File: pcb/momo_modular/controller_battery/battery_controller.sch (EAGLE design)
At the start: 33 parts, among them U1 XRP7659, U2 MAX1555, U3 MCP1702, U4 PIC24F16KA101-X_PSSOP, U5 FLASH8MSOP8

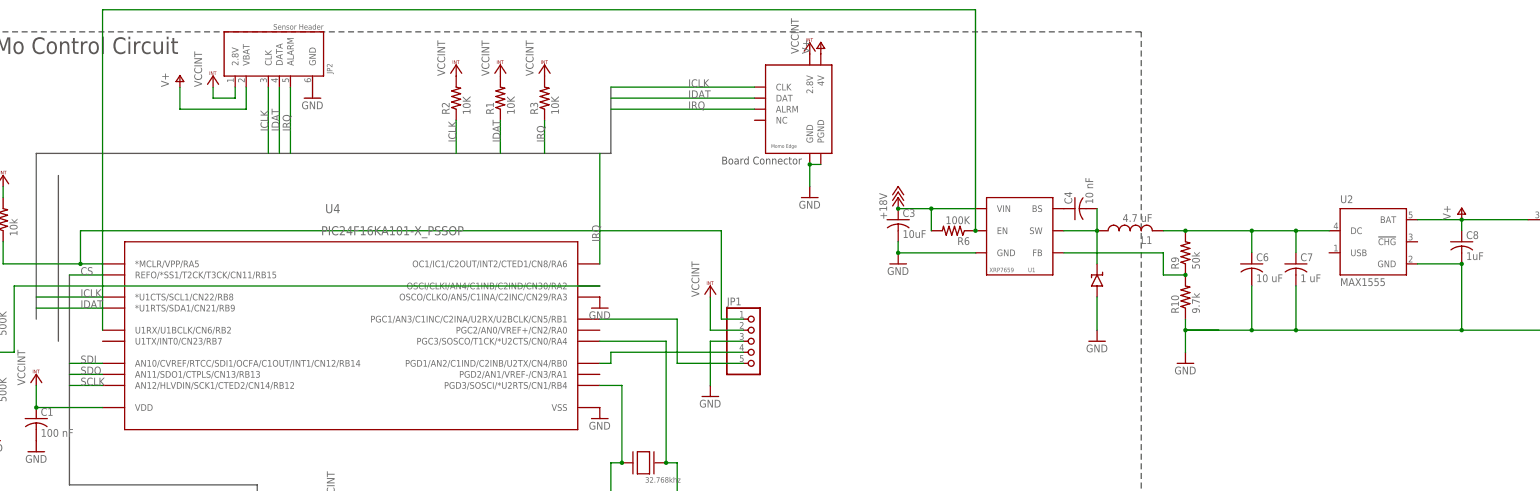
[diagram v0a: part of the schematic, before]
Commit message: Begin work on resource manager and revised task manager on pic24.  Started relaying out controller board and combining functionality.
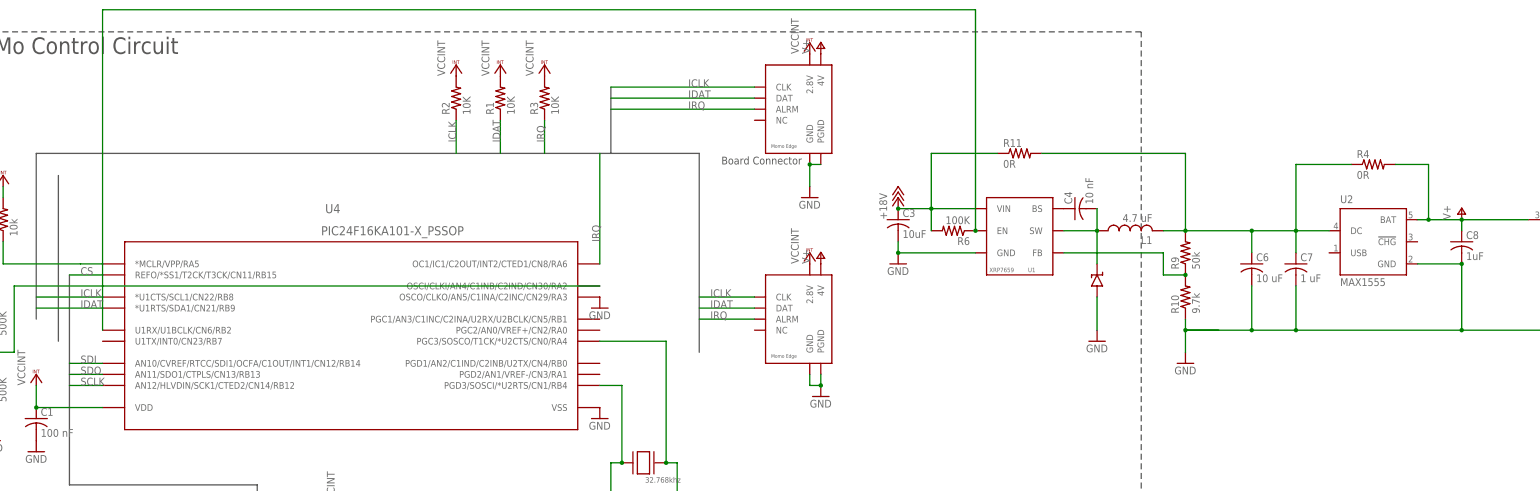
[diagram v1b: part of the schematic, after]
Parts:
- removed JP2: MOMO-SENSOR-HEADER, components:MOMO-SENSOR-HEADER
- added R11, R4: 0R, rcl:R-US_R0603
- JP1: value (none) -> MOMO-VERT-8M; device pinhead:PINHD-1X5 -> components:MOMO-VERT-8M
- renumbered JP4 to U$2, JP5 to U$1
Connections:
- removed net N$1: JP1.4, U4.PGD1/AN2/C1IND/C2INB/U2TX/CN4/RB0
- removed net N$2: JP1.5, U4.PGC1/AN3/C1INC/C2INA/U2RX/U2BCLK/CN5/RB1
- net +18V: now also R11.1
- net GND: now also JP1.GND, JP1.PGND; no longer JP1.3, JP2.GND
- net ICLK: now also JP1.CLK; no longer JP2.CLK
- net IDAT: now also JP1.DAT; no longer JP2.DATA
- net IRQ: now also JP1.ALRM; no longer JP2.ALARM
- net N$15: no longer JP1.1
- net N$5: now also R11.2, R4.1
- net V+: now also JP1.4V, R4.2; no longer JP2.VBAT
- net VCCINT: now also JP1.2.8V; no longer JP1.2, JP2.2.8V
